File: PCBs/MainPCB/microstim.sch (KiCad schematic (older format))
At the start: 113 parts, among them J1 Conn_02x08_Odd_Even, J2 Conn_Coaxial, J3 Conn_Coaxial, J6 Screw_Terminal_01x02, J7 Conn_Coaxial, J8 Screw_Terminal_01x02, J9 Conn_Coaxial, SW1 SW_Push, U1 Teensy3.5, U10 AD8276, U11 INA826, U12 DG509ACWE, U13 CC3-0512DF-E, U14 ISO7760, U15 ISO7341C, U16 L78L05_SO8, U17 AD5752, U18 AD7321, U19 AD1582, U2 CC3-0512DF-E, U20 OPA197, U21 AD8276, U22 INA826, U23 DG509ACWE, U3 ISO7760, U4 ISO7341C, U5 L78L05_SO8, U6 AD5752, U7 AD7321, U8 AD1582, U9 OPA197

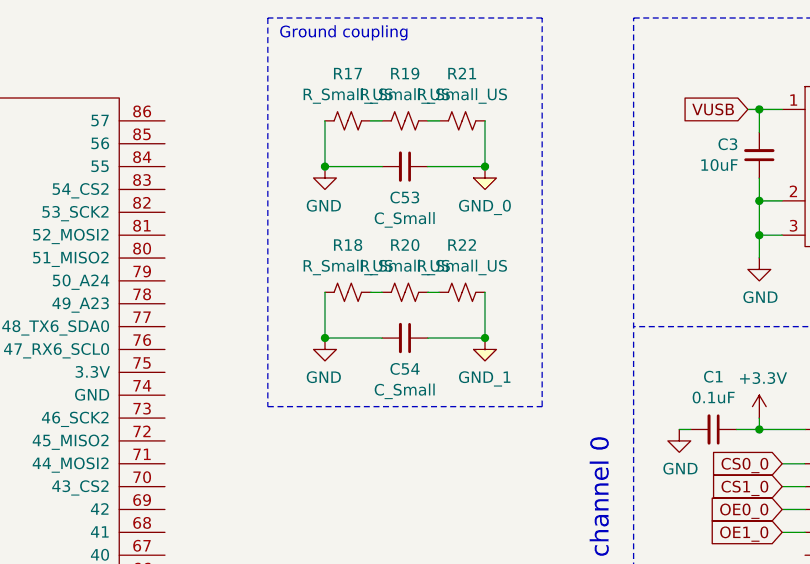
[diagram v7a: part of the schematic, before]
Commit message: changed name to stimjim. added logo-ish thing to board silkscreen. changed ground coupling caps/resistors slightly. renamed a bunch of stuff and replaced most instances of word microstim with stimjim
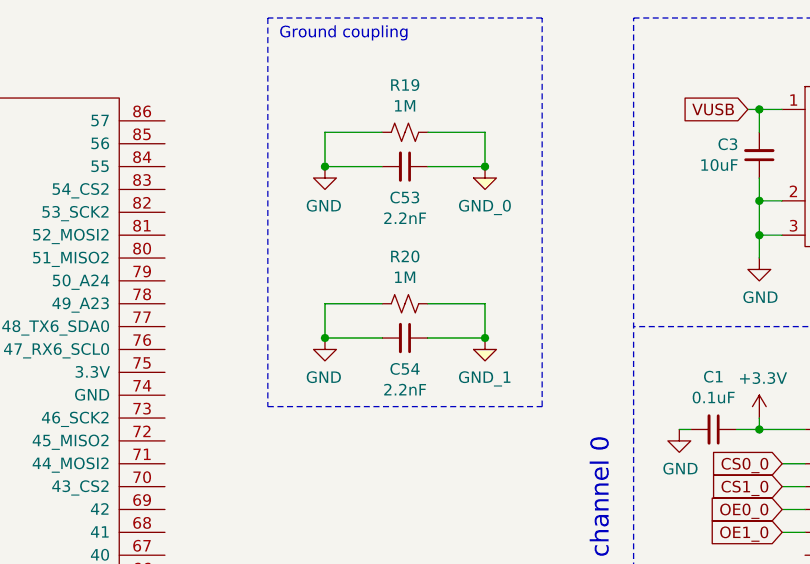
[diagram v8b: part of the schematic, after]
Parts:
- removed R17, R18, R21, R22: R_Small_US, Resistor_SMD:R_1210_3225Metric_Pad1.42x2.65mm_HandSolder, symbol Device:R_Small_US
- C53, C54: value C_Small -> 2.2nF; footprint Capacitor_THT:C_Disc_D12.5mm_W5.0mm_P10.00mm -> Capacitor_SMD:C_1210_3225Metric_Pad1.42x2.65mm_HandSolder
- R19, R20: value R_Small_US -> 1M
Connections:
- net GND: now also R19.2, R20.2
- net GND_0: now also R19.1
- net GND_1: now also R20.1
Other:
- moved on the sheet: R19, R20
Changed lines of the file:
@@
 	3250 4000 3750 4000
-$Comp
-L Device:R_Small_US R17
-U 1 1 5C780809
-P 4050 500
-F 0 "R17" V 3845 500 50  0000 C CNN
-F 1 "R_Small_US" V 3936 500 50  0000 C CNN
-F 2 "Resistor_SMD:R_1210_3225Metric_Pad1.42x2.65mm_HandSolder" H 4050 500 50  0001 C CNN
-F 3 "~" H 4050 500 50  0001 C CNN
-	1    4050 500
-	0    1    1    0
-$EndComp
 $Comp
 L Device:C_Small C53
@@
 P 4300 700
 F 0 "C53" V 4437 700 50  0000 C CNN
-F 1 "C_Small" V 4528 700 50  0000 C CNN
-F 2 "Capacitor_THT:C_Disc_D12.5mm_W5.0mm_P10.00mm" H 4300 700 50  0001 C CNN
+F 1 "2.2nF" V 4528 700 50  0000 C CNN
+F 2 "Capacitor_SMD:C_1210_3225Metric_Pad1.42x2.65mm_HandSolder" H 4300 700 50  0001 C CNN
 F 3 "~" H 4300 700 50  0001 C CNN
 	1    4300 700
 	0    1    1    0
 $EndComp
-$Comp
-L Device:R_Small_US R19
-U 1 1 5C782E14
-P 4300 500
-F 0 "R19" V 4095 500 50  0000 C CNN
-F 1 "R_Small_US" V 4186 500 50  0000 C CNN
-F 2 "Resistor_SMD:R_1210_3225Metric_Pad1.42x2.65mm_HandSolder" H 4300 500 50  0001 C CNN
-F 3 "~" H 4300 500 50  0001 C CNN
-	1    4300 500
-	0    1    1    0
-$EndComp
-$Comp
-L Device:R_Small_US R21
-U 1 1 5C7DBF6D
-P 4550 500
-F 0 "R21" V 4345 500 50  0000 C CNN
-F 1 "R_Small_US" V 4436 500 50  0000 C CNN
-F 2 "Resistor_SMD:R_1210_3225Metric_Pad1.42x2.65mm_HandSolder" H 4550 500 50  0001 C CNN
-F 3 "~" H 4550 500 50  0001 C CNN
-	1    4550 500
-	0    1    1    0
-$EndComp
-Wire Wire Line
-	4400 500  4450 500
-Wire Wire Line
-	4150 500  4200 500
 Wire Wire Line
 	4200 700  3950 700
 Wire Wire Line
-	3950 700  3950 500
+	3950 700  3950 550
 Wire Wire Line
 	4400 700  4650 700
 Wire Wire Line
-	4650 700  4650 500
+	4650 700  4650 550
 $Comp
 L power:GND #PWR01
@@
 Connection ~ 4650 700
 $Comp
-L Device:R_Small_US R18
-U 1 1 5CA53471
-P 4050 1250
-F 0 "R18" V 3845 1250 50  0000 C CNN
-F 1 "R_Small_US" V 3936 1250 50  0000 C CNN
-F 2 "Resistor_SMD:R_1210_3225Metric_Pad1.42x2.65mm_HandSolder" H 4050 1250 50  0001 C CNN
-F 3 "~" H 4050 1250 50  0001 C CNN
-	1    4050 1250
-	0    1    1    0
-$EndComp
-$Comp
 L Device:C_Small C54
 U 1 1 5CA53478
 P 4300 1450
 F 0 "C54" V 4437 1450 50  0000 C CNN
-F 1 "C_Small" V 4528 1450 50  0000 C CNN
-F 2 "Capacitor_THT:C_Disc_D12.5mm_W5.0mm_P10.00mm" H 4300 1450 50  0001 C CNN
+F 1 "2.2nF" V 4528 1450 50  0000 C CNN
+F 2 "Capacitor_SMD:C_1210_3225Metric_Pad1.42x2.65mm_HandSolder" H 4300 1450 50  0001 C CNN
 F 3 "~" H 4300 1450 50  0001 C CNN
 	1    4300 1450
@@
 L Device:R_Small_US R20
 U 1 1 5CA5347F
-P 4300 1250
-F 0 "R20" V 4095 1250 50  0000 C CNN
-F 1 "R_Small_US" V 4186 1250 50  0000 C CNN
-F 2 "Resistor_SMD:R_1210_3225Metric_Pad1.42x2.65mm_HandSolder" H 4300 1250 50  0001 C CNN
-F 3 "~" H 4300 1250 50  0001 C CNN
-	1    4300 1250
-	0    1    1    0
-$EndComp
-$Comp
-L Device:R_Small_US R22
-U 1 1 5CA53486
-P 4550 1250
-F 0 "R22" V 4345 1250 50  0000 C CNN
-F 1 "R_Small_US" V 4436 1250 50  0000 C CNN
-F 2 "Resistor_SMD:R_1210_3225Metric_Pad1.42x2.65mm_HandSolder" H 4550 1250 50  0001 C CNN
-F 3 "~" H 4550 1250 50  0001 C CNN
-	1    4550 1250
+P 4300 1300
+F 0 "R20" V 4095 1300 50  0000 C CNN
+F 1 "1M" V 4186 1300 50  0000 C CNN
+F 2 "Resistor_SMD:R_1210_3225Metric_Pad1.42x2.65mm_HandSolder" H 4300 1300 50  0001 C CNN
+F 3 "~" H 4300 1300 50  0001 C CNN
+	1    4300 1300
 	0    1    1    0
 $EndComp
 Wire Wire Line
-	4400 1250 4450 1250
-Wire Wire Line
-	4150 1250 4200 1250
-Wire Wire Line
 	4200 1450 3950 1450
 Wire Wire Line
-	3950 1450 3950 1250
+	3950 1450 3950 1300
 Wire Wire Line
 	4400 1450 4650 1450
 Wire Wire Line
-	4650 1450 4650 1250
+	4650 1450 4650 1300
 $Comp
 L power:GND #PWR03
@@
 Text Notes 3750 150  0    50   ~ 0
 Ground coupling
+$Comp
+L Device:R_Small_US R19
+U 1 1 5C782E14
+P 4300 550
+F 0 "R19" V 4095 550 50  0000 C CNN
+F 1 "1M" V 4186 550 50  0000 C CNN
+F 2 "Resistor_SMD:R_1210_3225Metric_Pad1.42x2.65mm_HandSolder" H 4300 550 50  0001 C CNN
+F 3 "~" H 4300 550 50  0001 C CNN
+	1    4300 550
+	0    1    1    0
+$EndComp
+Wire Wire Line
+	4400 1300 4650 1300
+Wire Wire Line
+	3950 1300 4200 1300
+Wire Wire Line
+	3950 550  4200 550
+Wire Wire Line
+	4400 550  4650 550
 $EndSCHEMATC
